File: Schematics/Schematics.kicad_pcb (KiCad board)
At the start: 2 copper layers, 85 x 90 mm, 18 parts, among them U1 TP4056, U2 BH1750, U3 BME688, U4 BU30TD3WG, U5 NRF52840-DONGLE, U6 LIS3DH

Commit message: Added almost(maybe even) finnal design and new gerber and drill files
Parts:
- added G***: LOGO, LOGO, F.Cu at (108.5, 81.0)
- moved U2 0.18 mm to (139.6, 139.4)
- moved H2 0.18 mm to (181.0, 64.0)
- moved R1 0.18 mm to (146.0, 116.3)
- moved R4 0.18 mm to (137.8, 94.8)
- moved U6 0.18 mm to (153.3, 120.7)
- moved U1 0.18 mm to (152.9, 60.3)
- moved C2 0.18 mm to (125.0, 88.4)
- moved D1 0.18 mm to (117.8, 83.8)
- moved H1 0.18 mm to (104.0, 64.0)
- moved R3 0.18 mm to (125.3, 94.8)
- moved U4 0.18 mm to (125.3, 84.2)
- moved U5 0.18 mm to (123.3, 106.0)
- moved H3 0.18 mm to (181.0, 146.0)
- moved BT1 0.18 mm to (167.1, 105.0)
- moved C1 0.18 mm to (129.2, 85.3)
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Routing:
- net /SDA: track 87.5 -> 69.0 mm
- net /SCL: track 56.1 -> 67.8 mm
- net /INT1: track 51.5 -> 62.6 mm
- net Net-(BT1-Pad2): track 67.0 -> 76.3 mm
- net Net-(D1-Pad1): track 42.4 -> 49.4 mm
- net +3V0: track 91.0 -> 96.1 mm
- net Net-(BT1-Pad1): track 35.3 -> 38.7 mm
- net VCC: track 48.0 -> 50.2 mm
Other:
- outline, holes or cut-outs redrawn
- board text added: "JLCJLCJLCJLC"

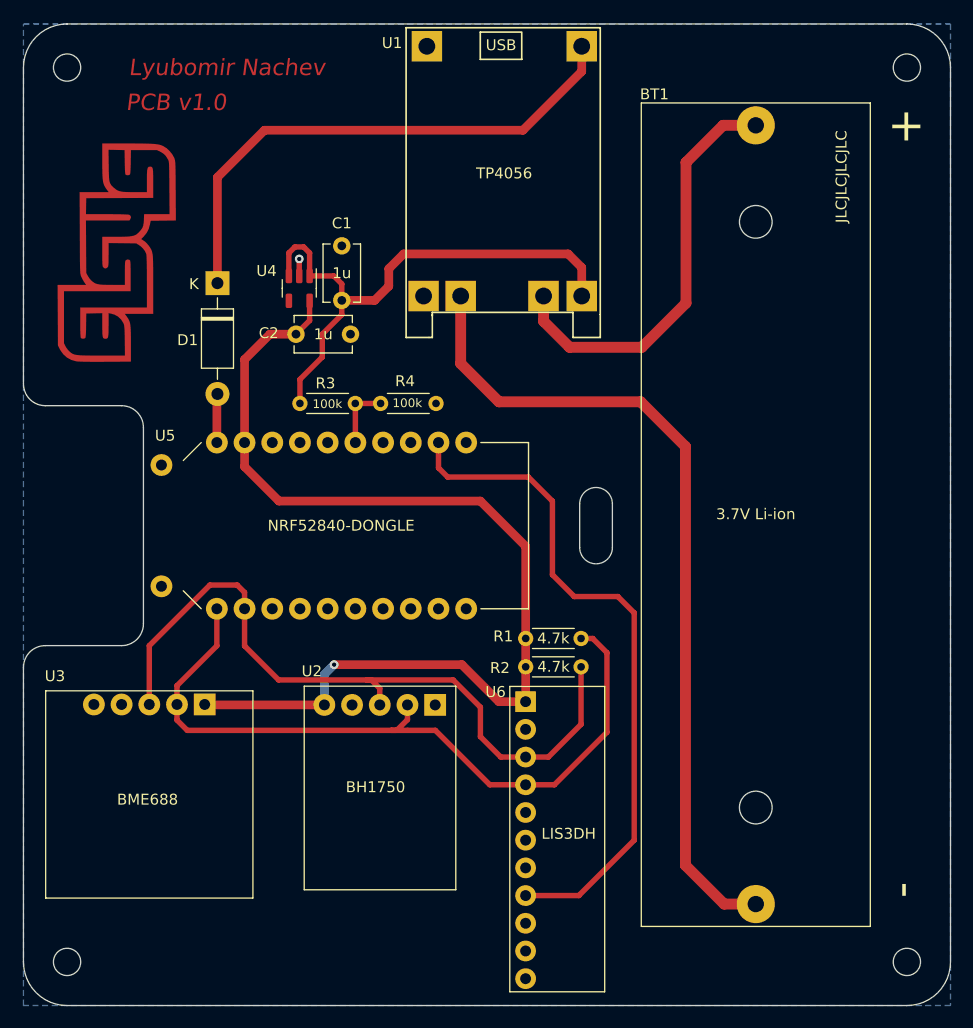
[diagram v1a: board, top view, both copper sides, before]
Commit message: Created final variant of the pcb, moved the schematic of the main node in this folder, modified the schematic of the main node
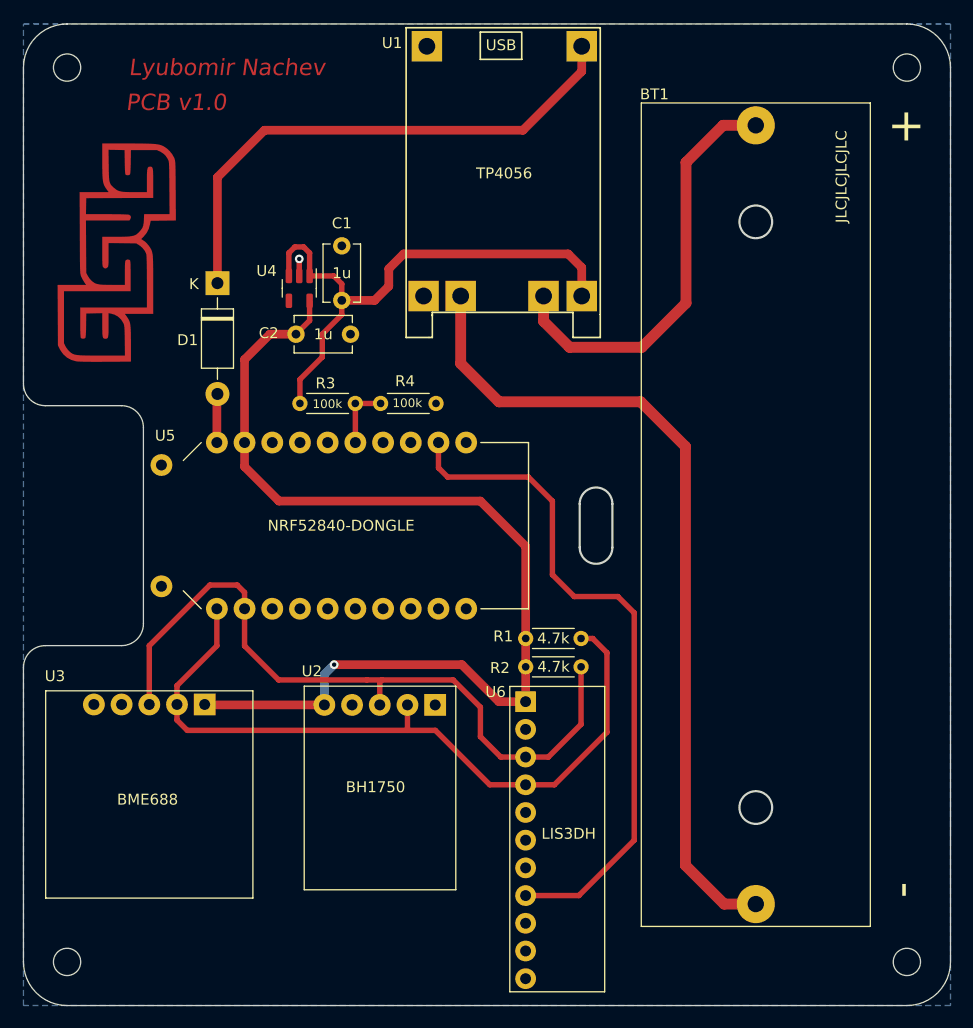
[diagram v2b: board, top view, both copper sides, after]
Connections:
- net GND renamed GNDD
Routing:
- net /SDA: track 69.0 -> 68.1 mm
- net /SCL: track 67.8 -> 67.1 mm
